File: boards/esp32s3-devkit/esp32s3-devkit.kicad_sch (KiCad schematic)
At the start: 37 parts, among them J1 Conn_01x17_Pin, J2 Conn_01x17_Pin, J3 USB_C_Receptacle_USB2.0_14P, Q1 Q_PMOS_GSD, SW1 ON/OFF, SW2 RESET, SW3 BOOT, U1 TPS630701RNMR, U2 ESP32-S3-WROOM-1, U3 USBLC6-2SC6

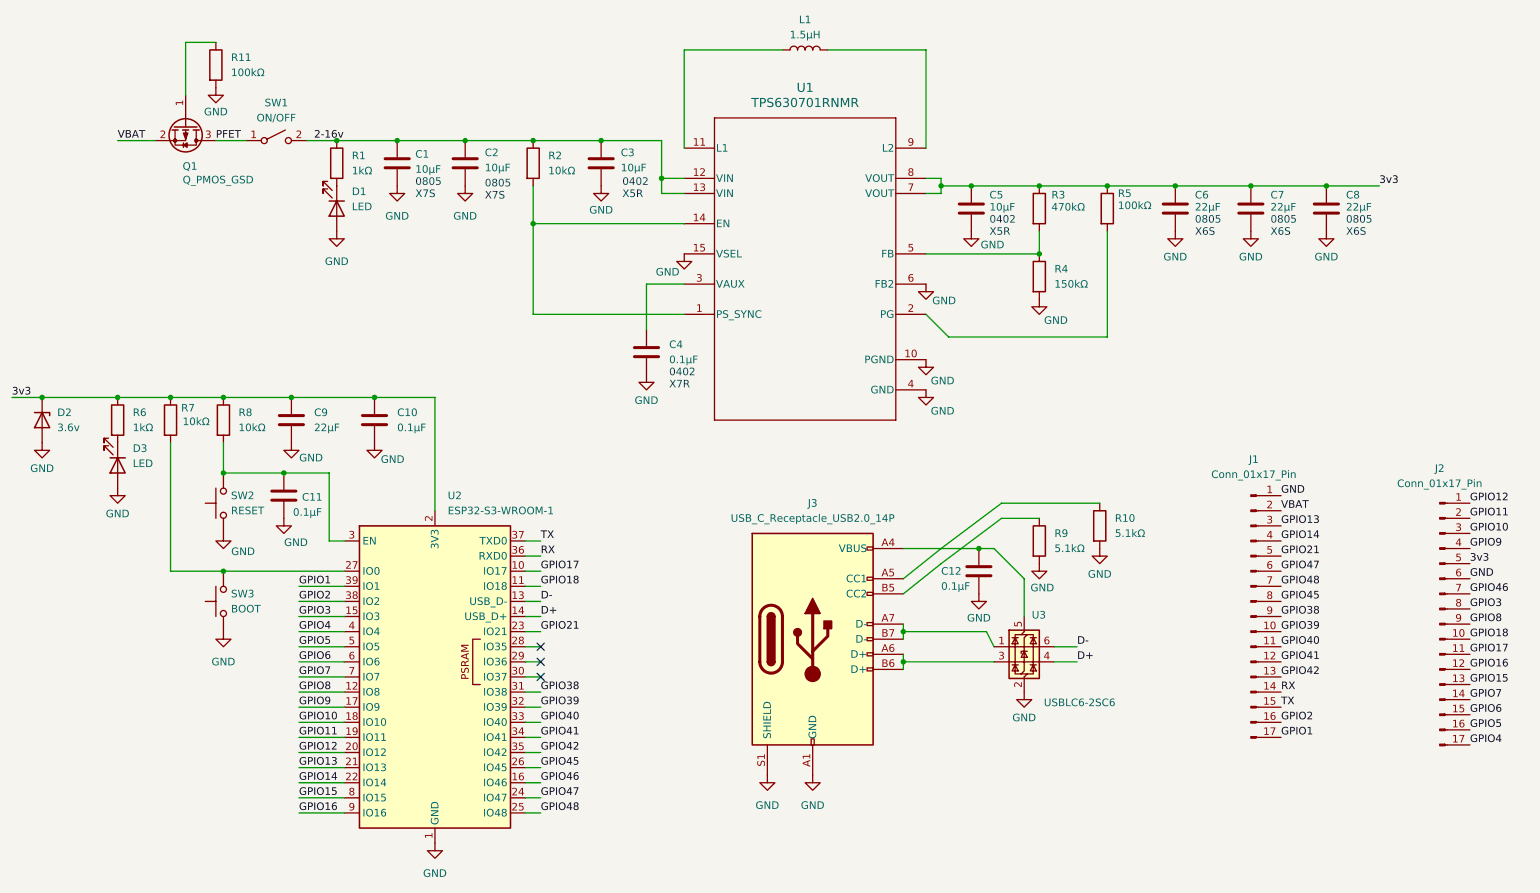
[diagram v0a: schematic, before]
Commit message: fix(esp32s3-devkit): add PWR_FLAG on VBAT for ERC (#94)
* fix(esp32s3-devkit): add PWR_FLAG on VBAT for ERC

Anchors KiCad ERC to the incoming supply net and keeps pcb/pro synced with schematic.

* fix(esp32s3-devkit): add ERC PWR_FLAGS on remaining supply nets

Adds additional PWR_FLAG instances and rewires schematic so KiCad ERC sees explicit power sources alongside GND anchors.

* fix(esp32s3-devkit): resolve TPS630701/USB ERC (PWR + symbol pin types)

- Add PWR_FLAG on the `2-16v` regulator input net (past the OR-ing) and align embedded TPS630701 with libs/symbols (VOUT/power pins, SIM props).
- Quote USB-C footprint as Connector_USB:* on J3 so KiCad resolves the nickname.
- Silence `lib_symbol_mismatch` in project ERC severities until embedded Connector artwork matches stock (KiCad cosmetic/stroke deltas only).

* fix(esp32s3-devkit): align USB-C HRO footprint shield pads with schematic S1

Fork Connector_USB footprint into libs: rename mounting pads SH→S1 so
USB_C_Receptacle_USB2.0_14P links cleanly; register HRO_TypeC_USB in fp-lib-table
and refresh embedded pcb pads after reassignment.

SBU pads A8/B8 remain optional for a future move to USB2.0_16P + no-connect SBUs.

* fix(esp32s3-devkit): migrate J3 USB-C to 16P symbol and Connector_USB footprint.

Use KiCad Connector USB‑C USB2 16P (A8/B8 SH) with the KiCad Connector_USB HRO footprint, remove the duplicated HRO footprint lib, refresh PCB pad SH naming, and add a small migration helper script.

* chore(esp32s3-devkit): remove one-off J3 USB migration script

The 14P→16P change is already applied in the schematic and PCB; the
helper script is no longer needed.
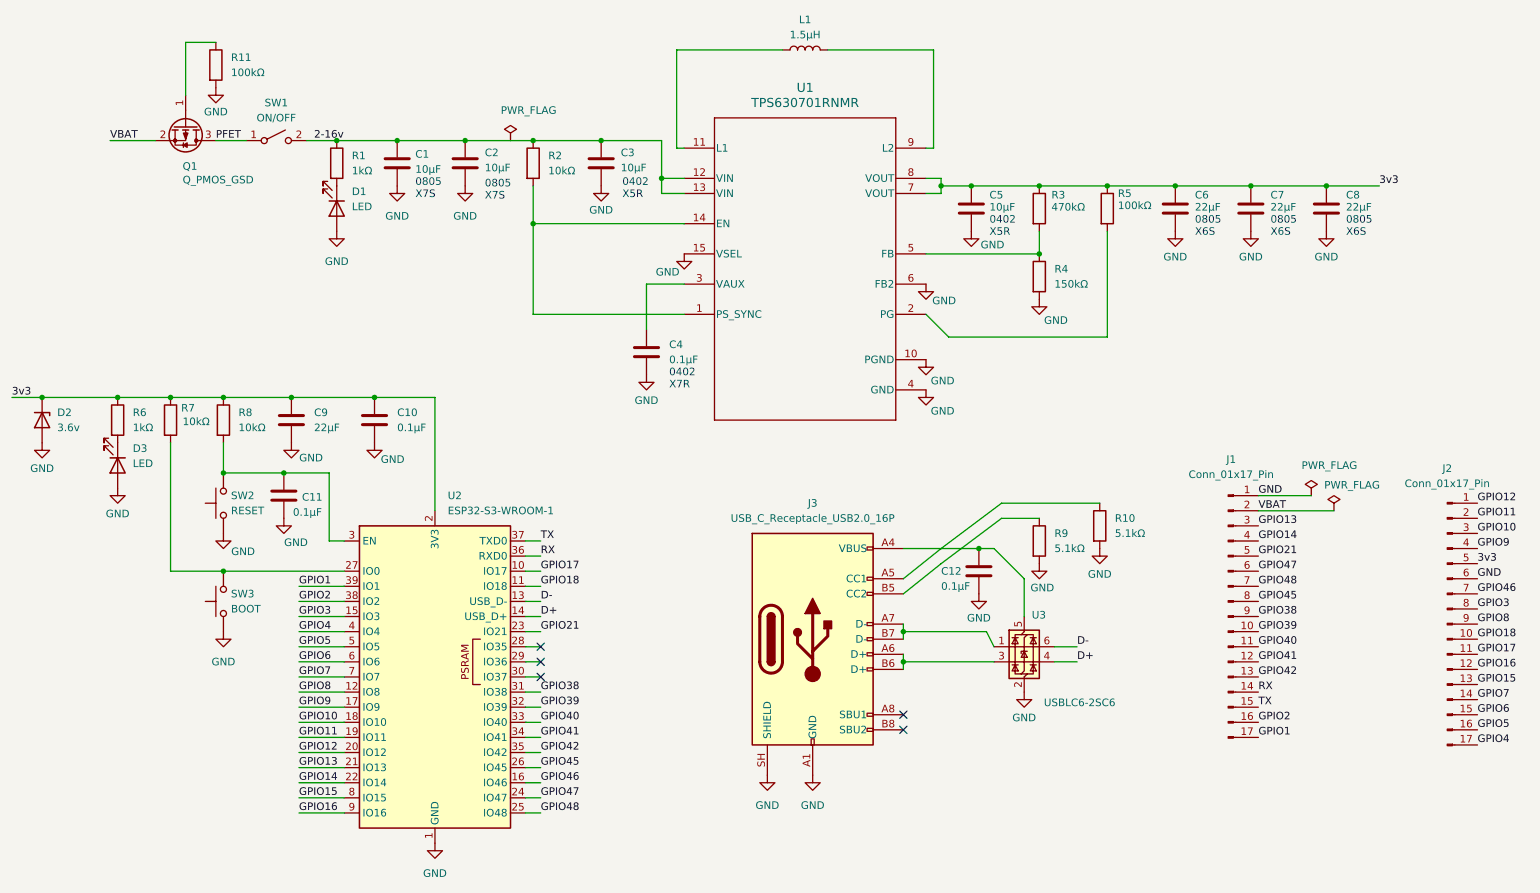
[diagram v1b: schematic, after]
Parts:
- J3: value USB_C_Receptacle_USB2.0_14P -> USB_C_Receptacle_USB2.0_16P; footprint USB_C_Receptacle_HRO_TYPE-C-31-M-12 -> Connector_USB:USB_C_Receptacle_HRO_TYPE-C-31-M-12; symbol Connector:USB_C_Receptacle_USB2.0_14P -> Connector:USB_C_Receptacle_USB2.0_16P
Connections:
- net GND: now also J3.SH (SHIELD); no longer J3.S1 (SHIELD)
- no-connect marks 3 -> 5
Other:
- moved on the sheet: J1, J2
